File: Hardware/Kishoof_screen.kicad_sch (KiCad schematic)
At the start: 5 parts, among them J1 Conn_01x02_Socket, J2 Conn_01x02_Socket, J3 Conn_01x02_Socket, J4 Conn_01x02_Socket

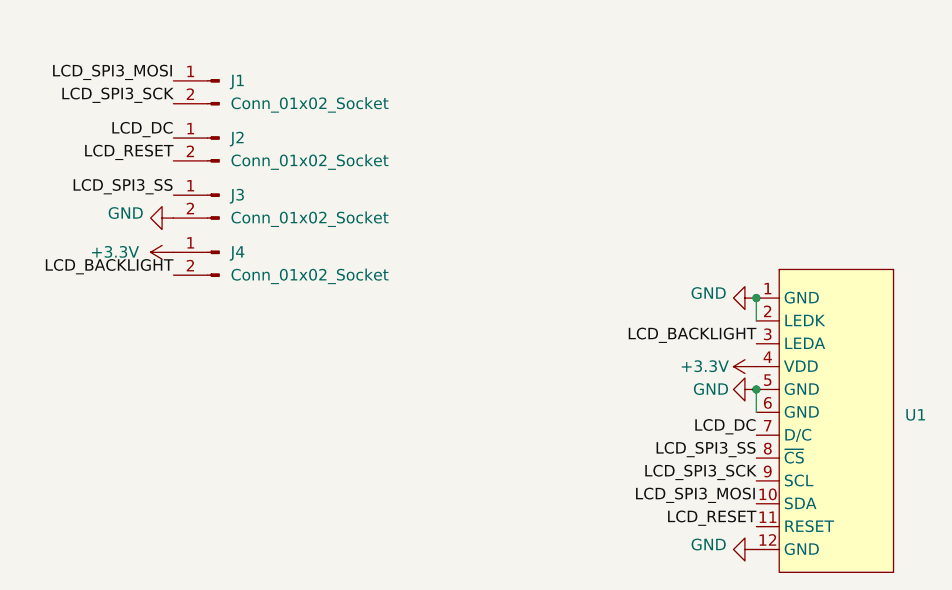
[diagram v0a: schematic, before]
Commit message: PCBs v1.0 ordered
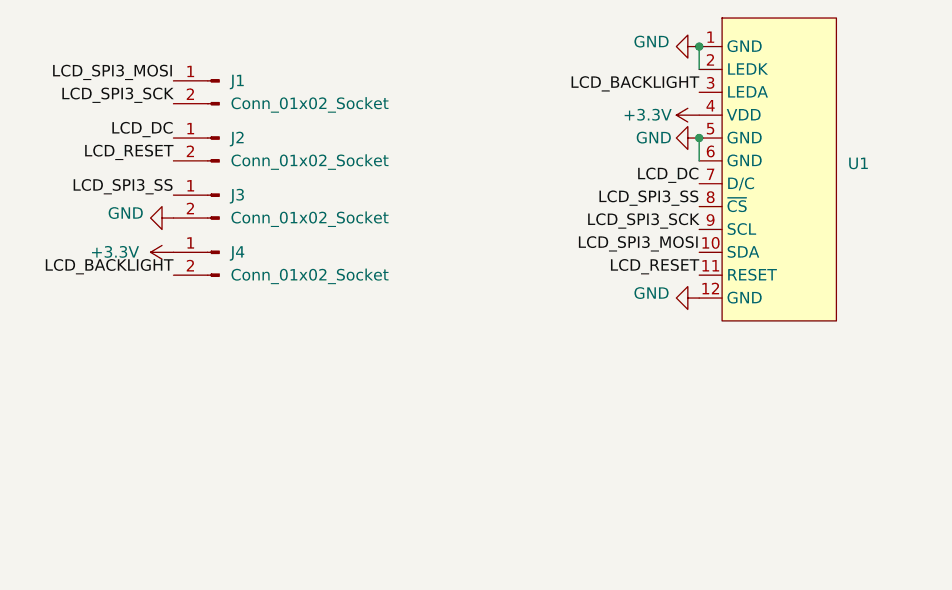
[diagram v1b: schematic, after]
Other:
- moved on the sheet: U1
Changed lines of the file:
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@@
 	(paper "A4")
 	(junction
-		(at 118.11 76.2)
+		(at 111.76 48.26)
 		(diameter 0)
 		(color 0 0 0 0)
 	)
 	(junction
-		(at 118.11 66.04)
+		(at 111.76 38.1)
 		(diameter 0)
 		(color 0 0 0 0)
@@
 	(wire
 		(pts
-			(xy 118.11 76.2) (xy 118.11 78.74)
+			(xy 111.76 48.26) (xy 111.76 50.8)
 		)
 		(stroke
@@
 	(wire
 		(pts
-			(xy 118.11 66.04) (xy 118.11 68.58)
+			(xy 111.76 38.1) (xy 111.76 40.64)
 		)
 		(stroke
@@
 	)
 	(label "LCD_RESET"
-		(at 118.11 91.44 180)
+		(at 111.76 63.5 180)
 		(fields_autoplaced yes)
 		(effects
@@
 	)
 	(label "LCD_BACKLIGHT"
-		(at 118.11 71.12 180)
+		(at 111.76 43.18 180)
 		(fields_autoplaced yes)
 		(effects
@@
 	)
 	(label "LCD_SPI3_MOSI"
-		(at 118.11 88.9 180)
+		(at 111.76 60.96 180)
 		(fields_autoplaced yes)
 		(effects
@@
 	)
 	(label "LCD_DC"
-		(at 118.11 81.28 180)
+		(at 111.76 53.34 180)
 		(fields_autoplaced yes)
 		(effects
@@
 	)
 	(label "LCD_SPI3_SCK"
-		(at 118.11 86.36 180)
+		(at 111.76 58.42 180)
 		(fields_autoplaced yes)
 		(effects
@@
 	)
 	(label "LCD_SPI3_SS"
-		(at 118.11 83.82 180)
+		(at 111.76 55.88 180)
 		(fields_autoplaced yes)
 		(effects
@@
 	(symbol
 		(lib_id "power:+3.3V")
-		(at 118.11 73.66 90)
+		(at 111.76 45.72 90)
 		(unit 1)
 		(exclude_from_sim no)
@@
 		(dnp no)
 		(property "Reference" "#PWR07"
-			(at 121.92 73.66 0)
+			(at 115.57 45.72 0)
 			(effects
 				(font
@@
 		)
 		(property "Value" "+3.3V"
-			(at 115.062 73.66 90)
+			(at 108.712 45.72 90)
 			(effects
 				(font
@@
 		)
 		(property "Footprint" ""
-			(at 118.11 73.66 0)
+			(at 111.76 45.72 0)
 			(effects
 				(font
@@
 		)
 		(property "Datasheet" ""
-			(at 118.11 73.66 0)
+			(at 111.76 45.72 0)
 			(effects
 				(font
@@
 		)
 		(property "Description" "Power symbol creates a global label with name \"+3.3V\""
-			(at 118.11 73.66 0)
+			(at 111.76 45.72 0)
 			(effects
 				(font
@@
 	(symbol
 		(lib_id "Mountjoy:Round_LCD")
-		(at 127 80.01 0)
+		(at 120.65 52.07 0)
 		(unit 1)
 		(exclude_from_sim no)
@@
 		(fields_autoplaced yes)
 		(property "Reference" "U1"
-			(at 134.62 79.0574 0)
+			(at 128.27 51.1174 0)
 			(effects
 				(font
@@
 		)
 		(property "Value" "~"
-			(at 134.62 80.9625 0)
+			(at 128.27 53.0225 0)
 			(effects
 				(font
@@
 		)
 		(property "Footprint" "Custom_Footprints:Round_LCD"
-			(at 127.254 99.06 0)
+			(at 120.904 71.12 0)
 			(effects
 				(font
@@
 		)
 		(property "Datasheet" ""
-			(at 123.19 64.77 0)
+			(at 116.84 36.83 0)
 			(effects
 				(font
@@
 		)
 		(property "Description" ""
-			(at 127 67.31 0)
+			(at 120.65 39.37 0)
 			(effects
 				(font
@@
 	(symbol
 		(lib_id "power:GND")
-		(at 118.11 93.98 270)
+		(at 111.76 66.04 270)
 		(unit 1)
 		(exclude_from_sim no)
@@
 		(dnp no)
 		(property "Reference" "#PWR03"
-			(at 111.76 93.98 0)
+			(at 105.41 66.04 0)
 			(effects
 				(font
@@
 		)
 		(property "Value" "GND"
-			(at 114.808 93.472 90)
+			(at 108.458 65.532 90)
 			(effects
 				(font
@@
 		)
 		(property "Footprint" ""
-			(at 118.11 93.98 0)
+			(at 111.76 66.04 0)
 			(effects
 				(font
@@
 		)
 		(property "Datasheet" ""
-			(at 118.11 93.98 0)
+			(at 111.76 66.04 0)
 			(effects
 				(font
@@
 		)
 		(property "Description" "Power symbol creates a global label with name \"GND\" , ground"
-			(at 118.11 93.98 0)
+			(at 111.76 66.04 0)
 			(effects
 				(font
@@
 	(symbol
 		(lib_id "power:GND")
-		(at 118.11 66.04 270)
+		(at 111.76 38.1 270)
 		(unit 1)
 		(exclude_from_sim no)
@@
 		(dnp no)
 		(property "Reference" "#PWR05"
-			(at 111.76 66.04 0)
+			(at 105.41 38.1 0)
 			(effects
 				(font
@@
 		)
 		(property "Value" "GND"
-			(at 114.808 65.532 90)
+			(at 108.458 37.592 90)
 			(effects
 				(font
@@
 		)
 		(property "Footprint" ""
-			(at 118.11 66.04 0)
+			(at 111.76 38.1 0)
 			(effects
 				(font
@@
 		)
 		(property "Datasheet" ""
-			(at 118.11 66.04 0)
+			(at 111.76 38.1 0)
 			(effects
 				(font
@@
 		)
 		(property "Description" "Power symbol creates a global label with name \"GND\" , ground"
-			(at 118.11 66.04 0)
+			(at 111.76 38.1 0)
 			(effects
 				(font
@@
 	(symbol
 		(lib_id "power:GND")
-		(at 118.11 76.2 270)
+		(at 111.76 48.26 270)
 		(unit 1)
 		(exclude_from_sim no)
@@
 		(dnp no)
 		(property "Reference" "#PWR06"
-			(at 111.76 76.2 0)
+			(at 105.41 48.26 0)
 			(effects
 				(font
@@
 		)
 		(property "Value" "GND"
-			(at 115.062 76.2 90)
+			(at 108.712 48.26 90)
 			(effects
 				(font
@@
 		)
 		(property "Footprint" ""
-			(at 118.11 76.2 0)
+			(at 111.76 48.26 0)
 			(effects
 				(font
@@
 		)
 		(property "Datasheet" ""
-			(at 118.11 76.2 0)
+			(at 111.76 48.26 0)
 			(effects
 				(font
@@
 		)
 		(property "Description" "Power symbol creates a global label with name \"GND\" , ground"
-			(at 118.11 76.2 0)
-			(effects
-				(font
+			(at 111.76 48.26 0)
+			(effects
+				(font
